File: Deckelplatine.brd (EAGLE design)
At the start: 110 x 75 mm, 67 parts, among them IC1 MAX1487EESA+, IC2 74HCT595D, IC3 74HCT595D, IC4 74HCT595D, IC5 74HCT595D, IC6 74HCT595D, J1 52808-2570, Q1 BC846BSMD, Q2 BC846BSMD, U1 LM2676S, X1 236-404, X2 233-502

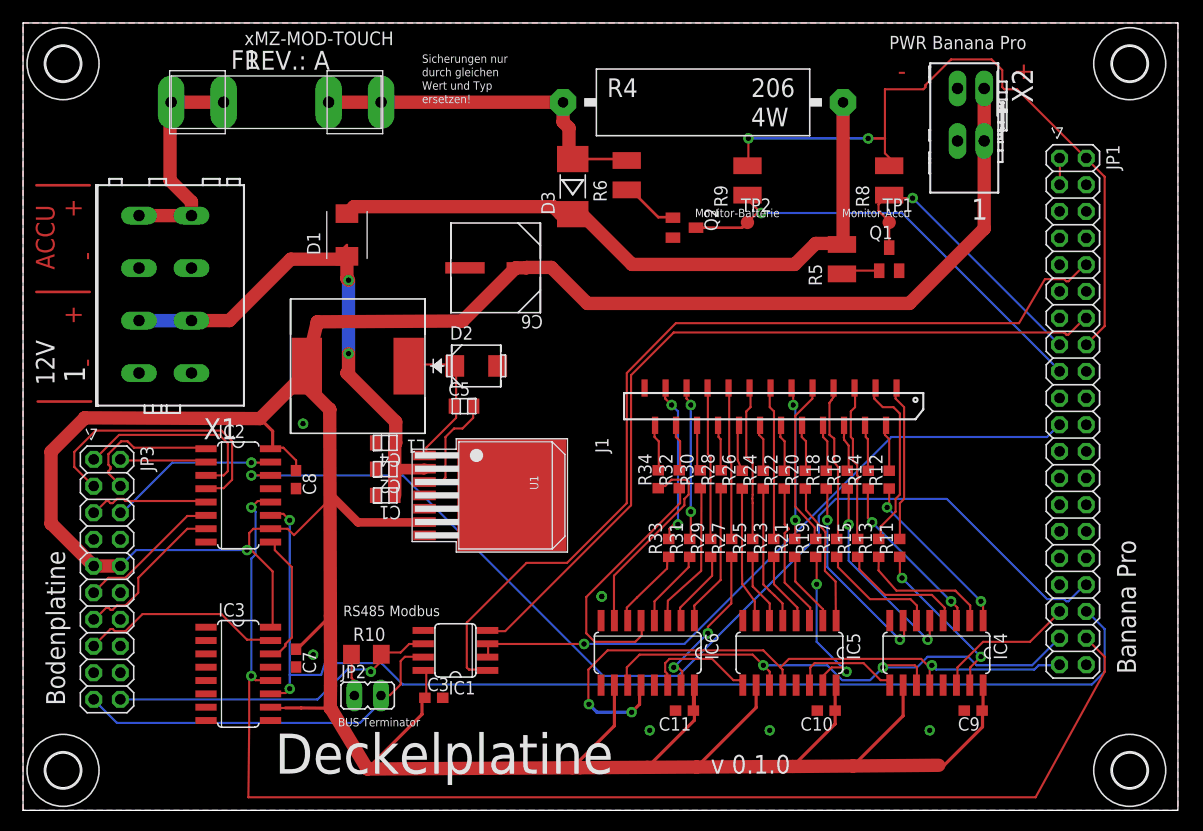
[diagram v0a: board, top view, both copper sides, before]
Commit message: Schaltregler überarbeitet, Teil 1
CIN angepasst, Größe stimmte nicht (zu klein).
Materialliste Farnell an Schaltplan "webench_design_4385517_7_60043841.pdf" angepasst.
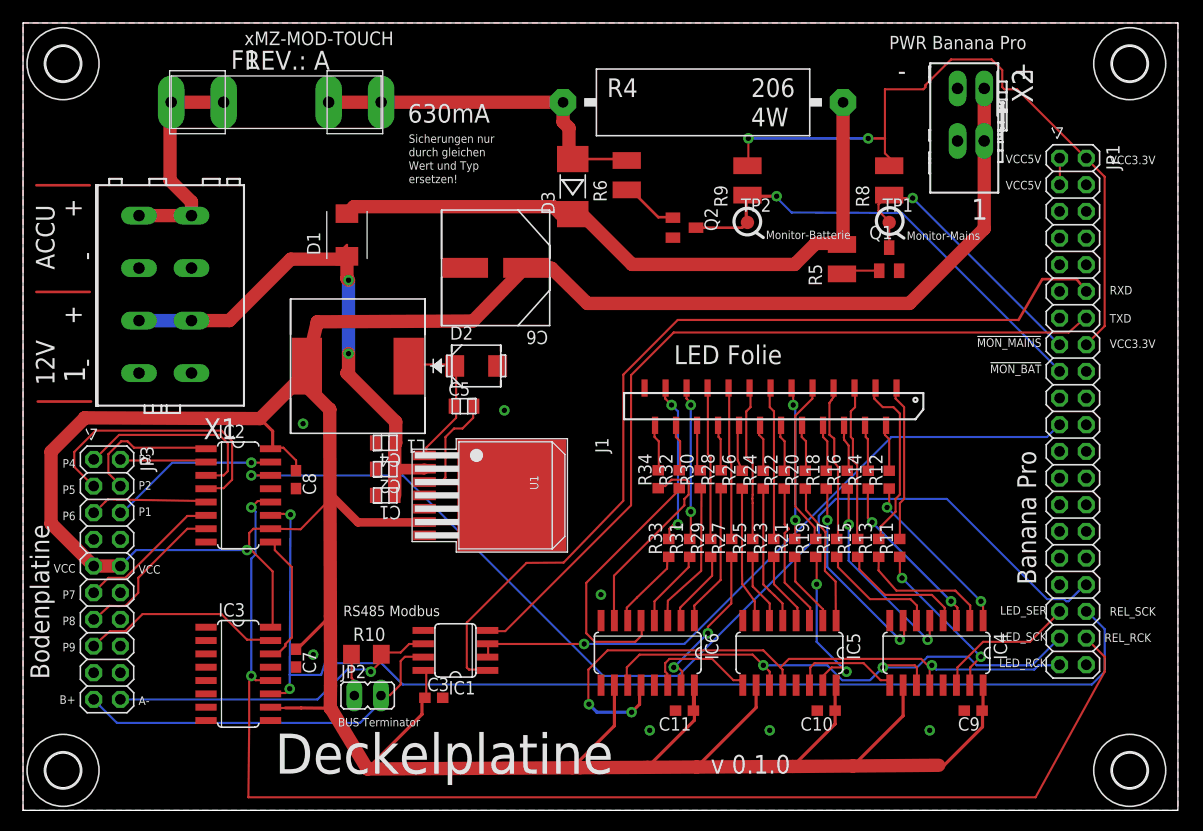
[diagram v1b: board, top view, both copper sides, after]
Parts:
- C1, C2: value 0.1uF -> 4.7 uF
- C4: value 0.1uF -> 100.0 nF
- C6: value 100uF 16v -> 180.0 uF; device AcceleratedDesigns_Lib:SM_RADIAL_8MM -> AcceleratedDesigns_Lib:SM_RADIAL_10MM
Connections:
- removed net N$1415: JP1.12
- net GND: now also JP1.10
- net RXD: now also JP1.12; no longer JP1.10
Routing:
- net !MON_BAT: track 43.8 -> 44.7 mm
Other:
- board text added: "!MON_BAT"
- board text added: "!MON_MAINS"
- board text added: "630mA"
- board text added: "A-"
- board text added: "B+"
- board text added: "LED Folie"
- board text added: "LED_RCK"
- board text added: "LED_SCK"
- board text added: "LED_SER"
- board text added: "Monitor-Mains"
- board text added: "P1"
- board text added: "P2"
- board text added: "P3"
- board text added: "P4"
- board text added: "P5"
- board text added: "P6"
- board text added: "P7"
- board text added: "P8"
- board text added: "P9"
- board text added: "REL_RCK"
- board text added: "REL_SCK"
- board text added: "RXD"
- board text added: "TXD"
- board text added: "VCC"
- board text added: "VCC3.3V"
- board text added: "VCC5V"
- board text removed: "Monitor-Accu"

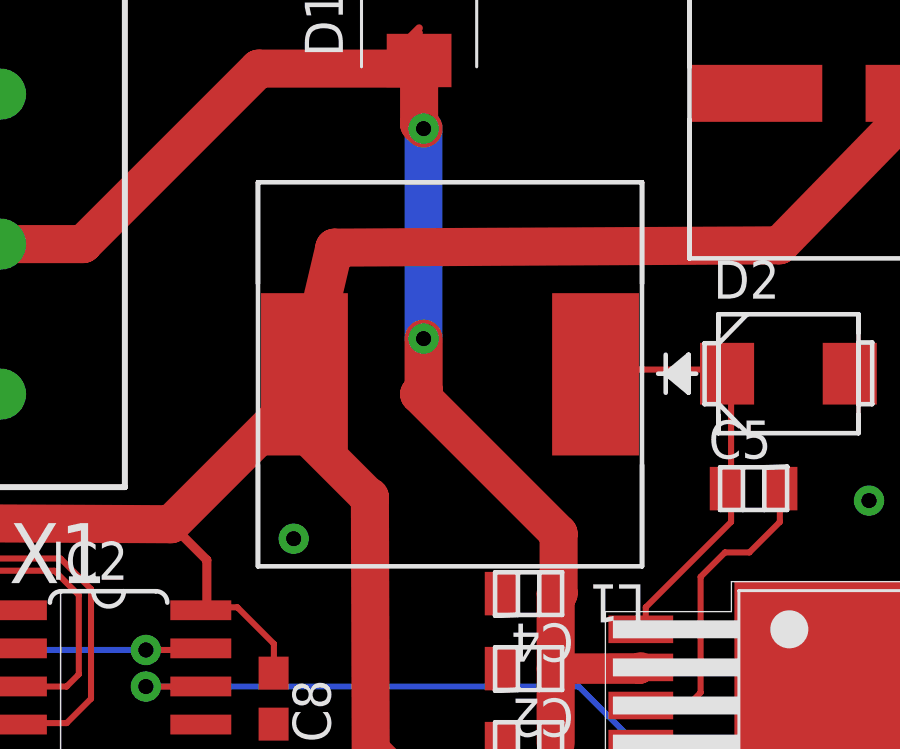
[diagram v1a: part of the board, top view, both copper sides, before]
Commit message: Nach 2. Bestellung bei Farnell
Schaltregler Induktion musste nochmals ausgewechselt werden da
die vorherige nur aus USA importierbar wäre.
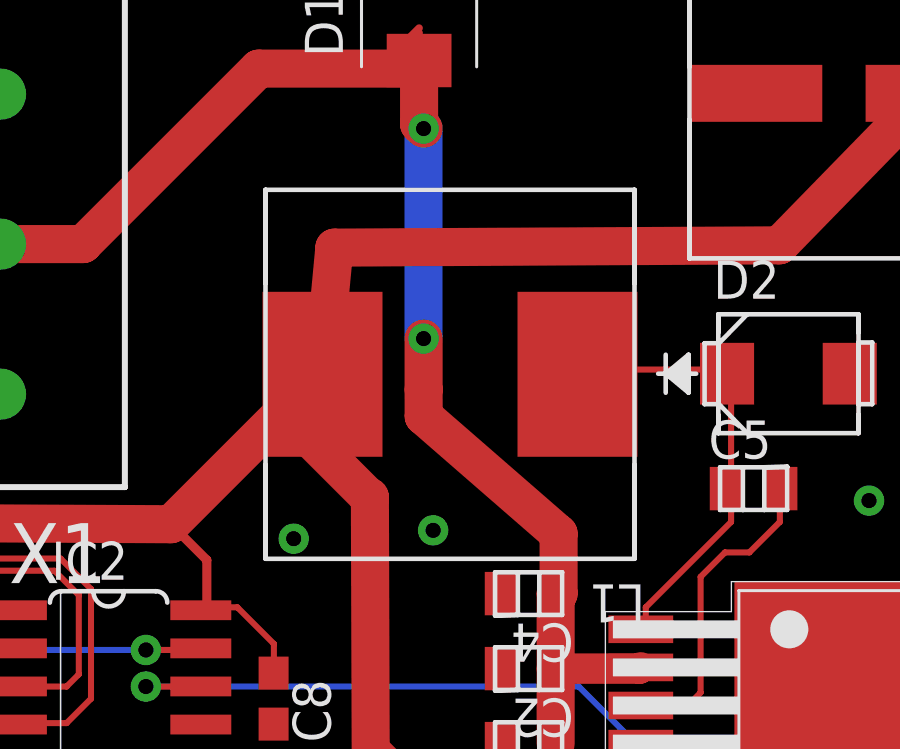
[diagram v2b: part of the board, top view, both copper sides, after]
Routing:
- net N$44: track 14.6 -> 15.1 mm
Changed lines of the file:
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@@
 <setting verticaltext="up"/>
 </settings>
-<grid distance="0.5" unitdist="mm" unit="mm" style="lines" multiple="1" display="yes" altdistance="0.1" altunitdist="mm" altunit="mm"/>
+<grid distance="0.05" unitdist="inch" unit="inch" style="lines" multiple="1" display="yes" altdistance="0.005" altunitdist="inch" altunit="inch"/>
 <layers>
 <layer number="1" name="Top" color="4" fill="1" visible="yes" active="yes"/>
@@
 <layer number="23" name="tOrigins" color="15" fill="1" visible="yes" active="yes"/>
 <layer number="24" name="bOrigins" color="15" fill="1" visible="yes" active="yes"/>
-<layer number="25" name="tNames" color="7" fill="1" visible="yes" active="yes"/>
+<layer number="25" name="tNames" color="7" fill="1" visible="no" active="yes"/>
 <layer number="26" name="bNames" color="7" fill="1" visible="no" active="yes"/>
 <layer number="27" name="tValues" color="7" fill="1" visible="no" active="yes"/>
@@
 <layer number="43" name="vRestrict" color="2" fill="10" visible="no" active="yes"/>
 <layer number="44" name="Drills" color="7" fill="1" visible="no" active="yes"/>
-<layer number="45" name="Holes" color="7" fill="1" visible="no" active="yes"/>
+<layer number="45" name="Holes" color="7" fill="1" visible="yes" active="yes"/>
 <layer number="46" name="Milling" color="3" fill="1" visible="no" active="yes"/>
 <layer number="47" name="Measures" color="7" fill="1" visible="no" active="yes"/>
@@
 <layer number="49" name="Reference" color="7" fill="1" visible="no" active="yes"/>
 <layer number="50" name="dxf" color="7" fill="1" visible="no" active="no"/>
-<layer number="51" name="tDocu" color="6" fill="1" visible="no" active="yes"/>
+<layer number="51" name="tDocu" color="6" fill="1" visible="yes" active="yes"/>
 <layer number="52" name="bDocu" color="7" fill="1" visible="no" active="yes"/>
 <layer number="53" name="tGND_GNDA" color="7" fill="9" visible="no" active="no"/>
@@
 </element>
 <element name="L1" library="AcceleratedDesigns_Lib" package="SRR1280" value="SRR1280-150M" x="31.88" y="42.31" rot="R180">
-<attribute name="MPN" value="SRR1280-150M" x="31.88" y="42.31" size="1.778" layer="27" rot="R180" display="off"/>
-<attribute name="MF" value="BOURNS" x="31.88" y="42.31" size="1.778" layer="27" rot="R180" display="off"/>
-<attribute name="OC_FARNELL" value="2336471" x="31.88" y="42.31" size="1.778" layer="27" rot="R180" display="off"/>
+<attribute name="MPN" value="MSS1278-153MLD" x="31.88" y="42.31" size="1.778" layer="27" rot="R180" display="off"/>
+<attribute name="MF" value="COILCRAFT" x="31.88" y="42.31" size="1.778" layer="27" rot="R180" display="off"/>
+<attribute name="OC_FARNELL" value="2288501" x="31.88" y="42.31" size="1.778" layer="27" rot="R180" display="off"/>
 <attribute name="IDC" value="5.0" x="31.88" y="42.31" size="1.778" layer="27" rot="R180" display="off"/>
 <attribute name="L" value="1.5E-5" x="31.88" y="42.31" size="1.778" layer="27" rot="R180" display="off"/>
@@
 <contactref element="JP1" pad="10"/>
 <via x="45.847" y="38.1" extent="1-16" drill="0.508"/>
+<via x="31.3182" y="37.1094" extent="1-16" drill="0.508"/>
 </signal>
 <signal name="VCC">
@@
 <wire x1="37.9984" y1="10.5664" x2="37.9984" y2="10.16" width="0.2032" layer="1"/>
 <wire x1="37.9984" y1="10.5664" x2="38.275" y2="10.7232" width="0.2032" layer="1"/>
-<wire x1="27.1272" y1="41.8592" x2="27.0286" y2="42.31" width="0.2032" layer="1"/>
+<wire x1="27.1272" y1="41.8592" x2="27.63" y2="42.31" width="0.2032" layer="1"/>
 <via x="21.336" y="24.7904" extent="1-16" drill="0.508"/>
 <wire x1="91.55" y1="68.762" x2="91.55" y2="63.762" width="1.27" layer="1"/>
@@
 <wire x1="47.8236" y1="51.7004" x2="42.8592" y2="46.609" width="1.27" layer="1"/>
 <wire x1="42.8592" y1="46.609" x2="28.0256" y2="46.5328" width="1.27" layer="1"/>
-<wire x1="28.0256" y1="46.5328" x2="27.0286" y2="42.31" width="1.27" layer="1"/>
+<wire x1="28.0256" y1="46.5328" x2="27.63" y2="42.31" width="1.27" layer="1"/>
 <wire x1="29.3624" y1="9.6266" x2="32.791396875" y2="3.937640625" width="1.27" layer="1"/>
 <wire x1="32.791396875" y1="3.937640625" x2="52.32405625" y2="4.054753125" width="1.27" layer="1"/>
@@
 <wire x1="30.58" y1="52.5" x2="30.85" y2="52.77" width="1.27" layer="1"/>
 <wire x1="30.85" y1="52.77" x2="30.85" y2="52.5" width="1.27" layer="1"/>
-<wire x1="30.85" y1="41.65" x2="35.5" y2="37" width="1.27" layer="1"/>
+<wire x1="31.0024" y1="40.9134" x2="35.5" y2="37" width="1.27" layer="1"/>
 <wire x1="35.5" y1="37" x2="35.5" y2="35" width="1.27" layer="1"/>
 <wire x1="35.5" y1="35" x2="35.4017" y2="35" width="1.27" layer="1"/>
@@
 <via x="31" y="43.5" extent="1-16" drill="0.508"/>
 <wire x1="31" y1="43.5" x2="31" y2="41.8" width="1.27" layer="1"/>
-<wire x1="31" y1="41.8" x2="30.85" y2="41.65" width="1.27" layer="1"/>
+<wire x1="31" y1="41.8" x2="31.0024" y2="40.9134" width="1.27" layer="1"/>
 <wire x1="30.85" y1="53.69" x2="30.5" y2="53.34" width="0.254" layer="1"/>
 <wire x1="30.85" y1="53.85" x2="30.85" y2="56.84" width="0" layer="19" extent="1-1"/>
@@
 <wire x1="41.2496" y1="38.4048" x2="41.0983" y2="38.5" width="0.2032" layer="1"/>
 <wire x1="41.0464" y1="42.4688" x2="36.7792" y2="42.4688" width="0.2032" layer="1"/>
-<wire x1="36.7792" y1="42.4688" x2="36.7314" y2="42.31" width="0.2032" layer="1"/>
+<wire x1="36.7792" y1="42.4688" x2="36.13" y2="42.31" width="0.2032" layer="1"/>
 <wire x1="41.0464" y1="42.4688" x2="41.1153" y2="42.33" width="0.2032" layer="1"/>
 </signal>

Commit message: Datasheet Shift Register
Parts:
- moved D1 5.64 mm to (26.8, 50.9), turned to 180 degrees
- moved C8 2.26 mm to (25.5, 33.7)
- moved C7 2.18 mm to (25.5, 16.6)
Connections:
- net LED_RCK renamed LED_ST_CP
- net LED_SCK renamed LED_SH_CP
- net LED_SER renamed LED_DS
- net REL_RCK renamed REL_ST_CP
- new net REL_DS: JP1.34
- new net REL_SH_CP: JP1.36
- net GND: now also D2.A; no longer D2.2
- net N$44: now also D2.C; no longer D2.1
- net REL_SCK: no longer JP1.36
- net REL_SER: no longer JP1.34
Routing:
- net N$3: track 12.9 -> 17.6 mm, vias 0 -> 2
- net 12V_VIN: track 116.7 -> 112.6 mm
- net GND: track 0.00 -> 2.21 mm, vias 8 -> 7
- net VCC: track 358.6 -> 356.5 mm
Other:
- board text added: "LED_DS"
- board text added: "LED_SH_CP"
- board text added: "LED_ST_CP"
- board text added: "REL_DS"
- board text added: "REL_SH_CP"
- board text added: "REL_ST_CP"
- board text added: "xMZ-Mod-Touch"
- board text removed: "LED_RCK"
- board text removed: "LED_SCK"
- board text removed: "LED_SER"
- board text removed: "REL_RCK"
- board text removed: "REL_SCK"
- board text removed: "REV.: A"
- board text removed: "xMZ-MOD-TOUCH"

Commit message: Zwischen Commit Änderungen leider nicht mehr klar
Leider habe ich vergessen welche Änderungen dieser Commit mit sich brachte.
Desshalb sollte dieser komplett ignoriert werden.
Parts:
- C10, C11, C7, C8, C9: value 100n -> 0.1uF
- C4: value 100.0 nF -> 0.1uF
- X1: value 236-404 -> 236-406/000-023; device con-wago_236:P-236-404 -> con-wago_236:P-236-406
- moved F1 12.7 mm to (36.8, 67.5)
- moved X1 5.08 mm to (14.0, 54.1)
- moved C3 0.90 mm to (39.3, 11.6)
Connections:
- removed net REL_SCK: IC2.11, IC3.11
- removed net REL_SER: IC2.14
- new net LED_!OE: IC4.13, IC5.13, IC6.13, JP1.31
- new net REL_!OE: IC2.13, IC3.13, JP1.32
- net 12V_VIN: now also X1.L4.1, X1.L4.2
- net ACCU+: now also X1.L6.1, X1.L6.2; no longer X1.L4.1, X1.L4.2
- net GND: now also X1.L5.1, X1.L5.2; no longer IC2.13, IC3.13, IC4.13, IC5.13, IC6.13
- net REL_DS: now also IC2.14
- net REL_SH_CP: now also IC2.11, IC3.11
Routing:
- net REL_!OE: track 0.00 -> 138.1 mm, vias 0 -> 2
- net REL_SH_CP: track 0.00 -> 106.9 mm, vias 0 -> 2
- net REL_SCK: track 106.7 -> 0.00 mm, vias 2 -> 0
- net REL_SER: track 102.0 -> 0.00 mm, vias 1 -> 0
- net REL_DS: track 0.00 -> 101.9 mm, vias 0 -> 1
- net LED_!OE: track 0.00 -> 50.8 mm, vias 0 -> 3
- net 12V_VIN: track 112.6 -> 132.1 mm
- net ACCU+: track 55.1 -> 41.7 mm
- net VCC: track 356.5 -> 347.8 mm, vias 1 -> 0
- net GND: track 2.21 -> 8.31 mm, vias 7 -> 10
- net REL_ST_CP: track 124.8 -> 122.5 mm
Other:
- board text added: "Con. Banana Pro"
- board text added: "Con. Bodenplatine"
- board text added: "LED SH_CP"
- board text added: "LED ST_CP"
- board text removed: "Banana Pro"
- board text removed: "Bodenplatine"
- board text removed: "LED_SH_CP"
- board text removed: "LED_ST_CP"
